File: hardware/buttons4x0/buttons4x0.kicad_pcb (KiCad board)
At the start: 2 copper layers, 48 x 18 mm, 11 parts, among them J1 Conn_01x05_Pin, SW1 Capacitive_Button, SW2 Capacitive_Button, SW3 Capacitive_Button, SW4 Capacitive_Button

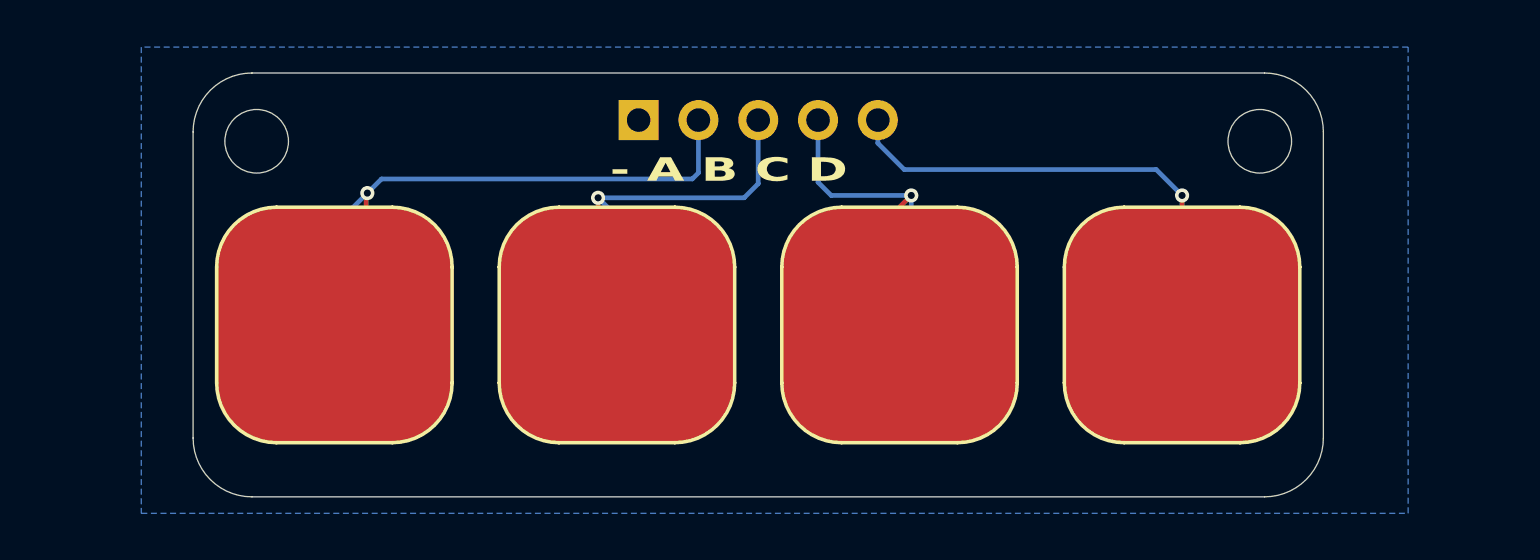
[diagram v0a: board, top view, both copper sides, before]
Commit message: fix spacing to allow tiling a bit better
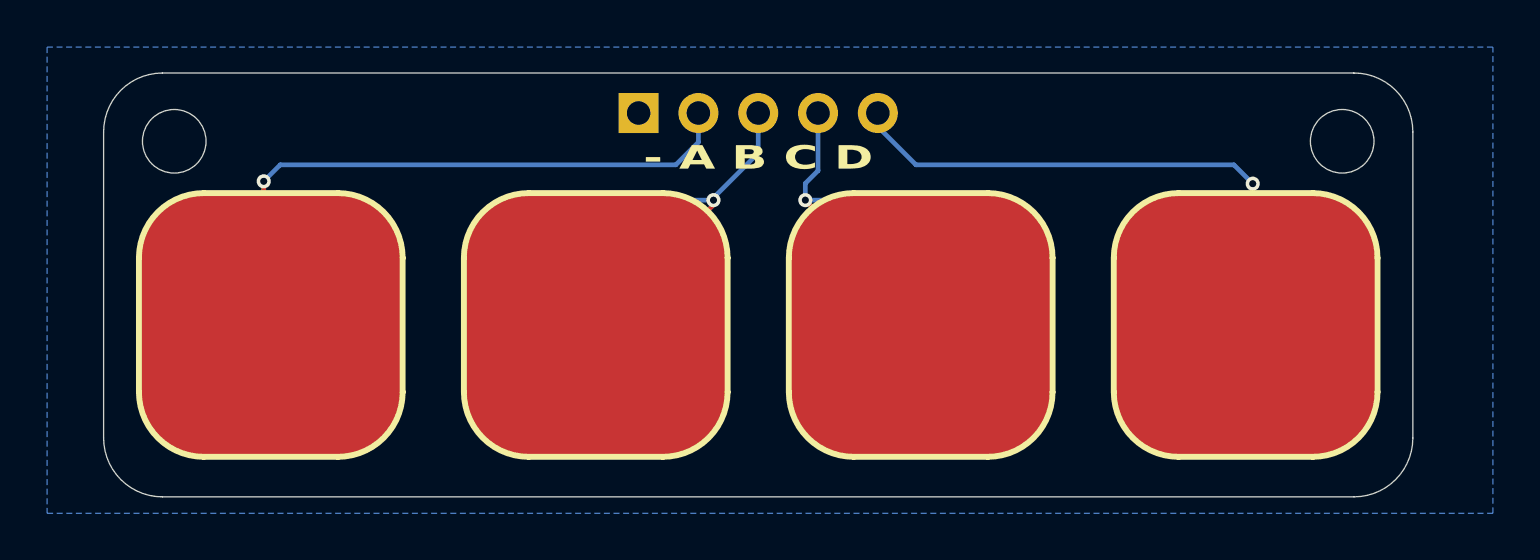
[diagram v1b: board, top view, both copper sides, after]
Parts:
- SW1, SW2, SW3, SW4: footprint todbot_stuff:Pad-CapTouch-10mm-roundrect -> todbot_stuff:Pad-CapTouch-11_2mm-roundrect
- moved H1 3.50 mm to (76.4, 51.4)
- moved H2 3.50 mm to (126.0, 51.4)
- moved R1 3.01 mm to (80.2, 57.0)
- moved R4 3.01 mm to (122.2, 57.0)
- moved SW1 2.70 mm to (80.5, 59.2)
- moved SW4 2.70 mm to (121.9, 59.2)
- moved R2 1.02 mm to (94.2, 57.0)
- moved R3 1.02 mm to (108.2, 57.0)
- moved SW2 0.90 mm to (94.3, 59.2)
- moved SW3 0.90 mm to (108.1, 59.2)
- moved J1 0.30 mm to (96.1, 50.2)
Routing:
- net Net-(J1-Pin_2): track 25.2 -> 29.0 mm
- net Net-(J1-Pin_4): track 15.1 -> 18.6 mm
- net Net-(J1-Pin_5): track 23.7 -> 26.1 mm
- net Net-(J1-Pin_3): track 18.4 -> 17.3 mm
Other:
- board size 48 x 18 mm -> 55.6 x 18 mm
